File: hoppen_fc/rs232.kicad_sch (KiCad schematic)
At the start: 7 parts, among them U7 SP3223

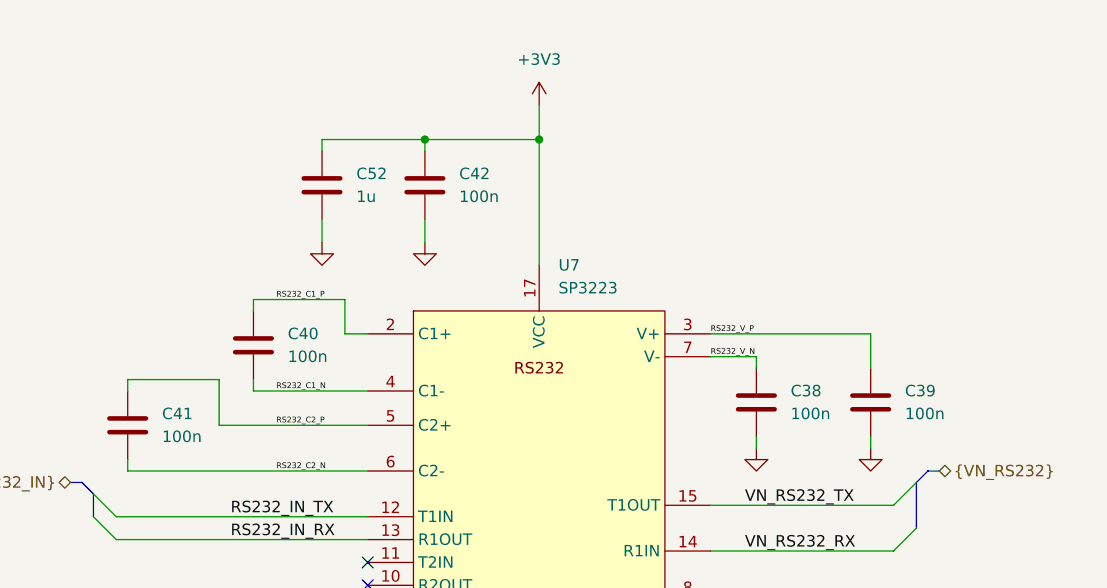
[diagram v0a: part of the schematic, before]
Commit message: finished adding lcsc numbers
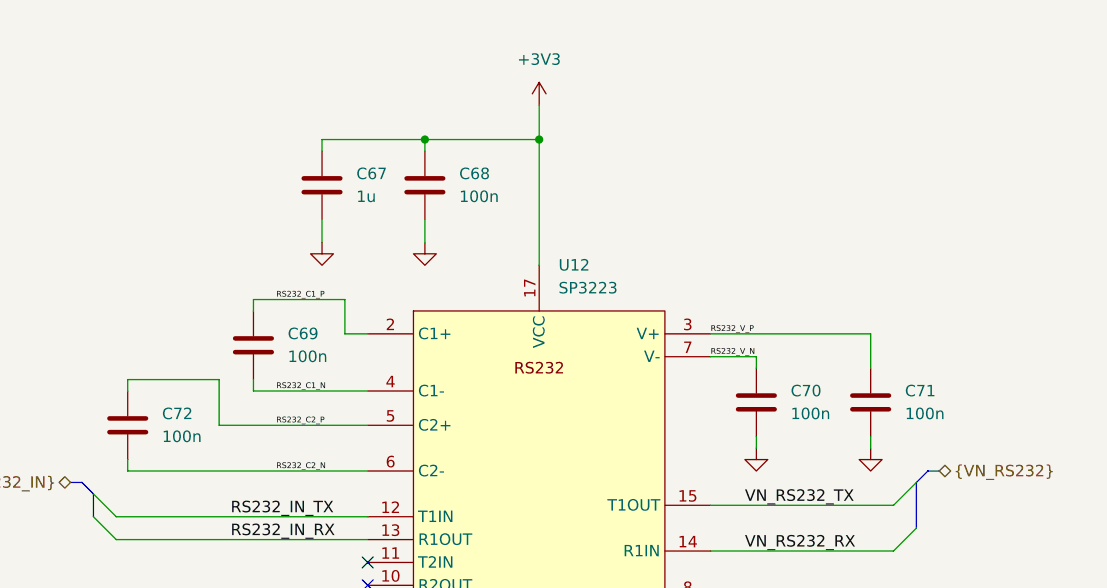
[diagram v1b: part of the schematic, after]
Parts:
- C67: renamed from C52; LCSC (none) -> C15849
- C68: renamed from C42; LCSC (none) -> C307331
- C69: renamed from C40; LCSC (none) -> C307331
- C70: renamed from C38; LCSC (none) -> C307331
- C71: renamed from C39; LCSC (none) -> C307331
- C72: renamed from C41; LCSC (none) -> C307331
- renumbered U7 to U12
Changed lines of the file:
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@@
 		(dnp no)
 		(fields_autoplaced yes)
-		(property "Reference" "C41"
+		(property "Reference" "C72"
 			(at 97.79 90.1699 0)
 			(effects
@@
 			)
 		)
+		(property "LCSC" "C307331"
+			(at 93.98 91.44 0)
+			(effects
+				(font
+					(size 1.27 1.27)
+				)
+				(hide yes)
+			)
+		)
 		(pin "2"
 		)
@@
 			(project "hoppen_fc"
 				(path "/abe950a1-9eef-4508-9fd4-31d3e723e029/c85454e5-a89e-41eb-a5ed-71b4fc4cf13a/b20bfd16-8587-4ee2-a4b4-53d6b6d5b5b2"
-					(reference "C41")
+					(reference "C72")
 					(unit 1)
 				)
@@
 		(dnp no)
 		(fields_autoplaced yes)
-		(property "Reference" "C40"
+		(property "Reference" "C69"
 			(at 111.76 81.2799 0)
 			(effects
@@
 			)
 		)
+		(property "LCSC" "C307331"
+			(at 107.95 82.55 0)
+			(effects
+				(font
+					(size 1.27 1.27)
+				)
+				(hide yes)
+			)
+		)
 		(pin "2"
 		)
@@
 			(project "hoppen_fc"
 				(path "/abe950a1-9eef-4508-9fd4-31d3e723e029/c85454e5-a89e-41eb-a5ed-71b4fc4cf13a/b20bfd16-8587-4ee2-a4b4-53d6b6d5b5b2"
-					(reference "C40")
+					(reference "C69")
 					(unit 1)
 				)
@@
 		(dnp no)
 		(fields_autoplaced yes)
-		(property "Reference" "#PWR051"
+		(property "Reference" "#PWR0105"
 			(at 176.53 100.33 0)
 			(effects
@@
 			(project "hoppen_fc"
 				(path "/abe950a1-9eef-4508-9fd4-31d3e723e029/c85454e5-a89e-41eb-a5ed-71b4fc4cf13a/b20bfd16-8587-4ee2-a4b4-53d6b6d5b5b2"
-					(reference "#PWR051")
+					(reference "#PWR0105")
 					(unit 1)
 				)
@@
 		(dnp no)
 		(fields_autoplaced yes)
-		(property "Reference" "C42"
+		(property "Reference" "C68"
 			(at 130.81 63.4999 0)
 			(effects
@@
 			)
 		)
+		(property "LCSC" "C307331"
+			(at 127 64.77 0)
+			(effects
+				(font
+					(size 1.27 1.27)
+				)
+				(hide yes)
+			)
+		)
 		(pin "2"
 		)
@@
 			(project "hoppen_fc"
 				(path "/abe950a1-9eef-4508-9fd4-31d3e723e029/c85454e5-a89e-41eb-a5ed-71b4fc4cf13a/b20bfd16-8587-4ee2-a4b4-53d6b6d5b5b2"
-					(reference "C42")
+					(reference "C68")
 					(unit 1)
 				)
@@
 		(dnp no)
 		(fields_autoplaced yes)
-		(property "Reference" "C38"
+		(property "Reference" "C70"
 			(at 167.64 87.6299 0)
 			(effects
@@
 			)
 		)
+		(property "LCSC" "C307331"
+			(at 163.83 88.9 0)
+			(effects
+				(font
+					(size 1.27 1.27)
+				)
+				(hide yes)
+			)
+		)
 		(pin "2"
 		)
@@
 			(project "hoppen_fc"
 				(path "/abe950a1-9eef-4508-9fd4-31d3e723e029/c85454e5-a89e-41eb-a5ed-71b4fc4cf13a/b20bfd16-8587-4ee2-a4b4-53d6b6d5b5b2"
-					(reference "C38")
+					(reference "C70")
 					(unit 1)
 				)
@@
 		(dnp no)
 		(fields_autoplaced yes)
-		(property "Reference" "#PWR050"
+		(property "Reference" "#PWR0104"
 			(at 163.83 100.33 0)
 			(effects
@@
 			(project ""
 				(path "/abe950a1-9eef-4508-9fd4-31d3e723e029/c85454e5-a89e-41eb-a5ed-71b4fc4cf13a/b20bfd16-8587-4ee2-a4b4-53d6b6d5b5b2"
-					(reference "#PWR050")
+					(reference "#PWR0104")
 					(unit 1)
 				)
@@
 		(dnp no)
 		(fields_autoplaced yes)
-		(property "Reference" "#PWR052"
+		(property "Reference" "#PWR0106"
 			(at 139.7 132.08 0)
 			(effects
@@
 			(project "hoppen_fc"
 				(path "/abe950a1-9eef-4508-9fd4-31d3e723e029/c85454e5-a89e-41eb-a5ed-71b4fc4cf13a/b20bfd16-8587-4ee2-a4b4-53d6b6d5b5b2"
-					(reference "#PWR052")
+					(reference "#PWR0106")
 					(unit 1)
 				)
@@
 		(dnp no)
 		(fields_autoplaced yes)
-		(property "Reference" "#PWR053"
+		(property "Reference" "#PWR0101"
 			(at 139.7 59.69 0)
 			(effects
@@
 			(project "hoppen_fc"
 				(path "/abe950a1-9eef-4508-9fd4-31d3e723e029/c85454e5-a89e-41eb-a5ed-71b4fc4cf13a/b20bfd16-8587-4ee2-a4b4-53d6b6d5b5b2"
-					(reference "#PWR053")
+					(reference "#PWR0101")
 					(unit 1)
 				)
@@
 		(dnp no)
 		(fields_autoplaced yes)
-		(property "Reference" "U7"
+		(property "Reference" "U12"
 			(at 141.8433 73.66 0)
 			(effects
@@
 			(project ""
 				(path "/abe950a1-9eef-4508-9fd4-31d3e723e029/c85454e5-a89e-41eb-a5ed-71b4fc4cf13a/b20bfd16-8587-4ee2-a4b4-53d6b6d5b5b2"
-					(reference "U7")
+					(reference "U12")
 					(unit 1)
 				)
@@
 		(dnp no)
 		(fields_autoplaced yes)
-		(property "Reference" "#PWR054"
+		(property "Reference" "#PWR0103"
 			(at 127 77.47 0)
 			(effects
@@
 			(project "hoppen_fc"
 				(path "/abe950a1-9eef-4508-9fd4-31d3e723e029/c85454e5-a89e-41eb-a5ed-71b4fc4cf13a/b20bfd16-8587-4ee2-a4b4-53d6b6d5b5b2"
-					(reference "#PWR054")
+					(reference "#PWR0103")
 					(unit 1)
 				)
@@
 		(dnp no)
 		(fields_autoplaced yes)
-		(property "Reference" "#PWR083"
+		(property "Reference" "#PWR0102"
 			(at 115.57 77.47 0)
 			(effects
@@
 			(project "hoppen_fc"
 				(path "/abe950a1-9eef-4508-9fd4-31d3e723e029/c85454e5-a89e-41eb-a5ed-71b4fc4cf13a/b20bfd16-8587-4ee2-a4b4-53d6b6d5b5b2"
-					(reference "#PWR083")
+					(reference "#PWR0102")
 					(unit 1)
 				)
@@
 		(dnp no)
 		(fields_autoplaced yes)
-		(property "Reference" "C39"
+		(property "Reference" "C71"
 			(at 180.34 87.6299 0)
 			(effects
@@
 			)
 		)
+		(property "LCSC" "C307331"
+			(at 176.53 88.9 0)
+			(effects
+				(font
+					(size 1.27 1.27)
+				)
+				(hide yes)
+			)
+		)
 		(pin "2"
 		)
@@
 			(project "hoppen_fc"
 				(path "/abe950a1-9eef-4508-9fd4-31d3e723e029/c85454e5-a89e-41eb-a5ed-71b4fc4cf13a/b20bfd16-8587-4ee2-a4b4-53d6b6d5b5b2"
-					(reference "C39")
+					(reference "C71")
 					(unit 1)
 				)
@@
 		(dnp no)
 		(fields_autoplaced yes)
-		(property "Reference" "C52"
+		(property "Reference" "C67"
 			(at 119.38 63.4999 0)
 			(effects
@@
 			)
 		)
+		(property "LCSC" "C15849"
+			(at 115.57 64.77 0)
+			(effects
+				(font
+					(size 1.27 1.27)
+				)
+				(hide yes)
+			)
+		)
 		(pin "1"
 		)
@@
 			(project "hoppen_fc"
 				(path "/abe950a1-9eef-4508-9fd4-31d3e723e029/c85454e5-a89e-41eb-a5ed-71b4fc4cf13a/b20bfd16-8587-4ee2-a4b4-53d6b6d5b5b2"
-					(reference "C52")
-					(unit 1)
-				)
+					(reference "C67")
+					(unit 1)
+				)

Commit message: ready for routing?
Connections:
- net RS232_nEN is gone; now on net RS232_C1_P: U12.1 (C1+)
- net +3V3: now also U12.16 (VCC); no longer U12.17 (VCC)
- net GND: now also U12.15 (GND); no longer U12.16 (GND)
- net RS232_C1_N: now also U12.3 (C1-); no longer U12.4 (C1-)
- net RS232_C1_P: no longer U12.2 (C1+)
- net RS232_C2_N: now also U12.5 (C2-); no longer U12.6 (C2-)
- net RS232_C2_P: now also U12.4 (C2+); no longer U12.5 (C2+)
- net RS232_IN_RX: now also U12.12 (R1OUT); no longer U12.13 (R1OUT)
- net RS232_IN_TX: now also U12.11 (T1IN); no longer U12.12 (T1IN)
- net RS232_V_N: now also U12.6 (V-); no longer U12.7 (V-)
- net RS232_V_P: now also U12.2 (V+); no longer U12.3 (V+)
- net VN_RS232_RX: now also U12.13 (R1IN); no longer U12.14 (R1IN)
- net VN_RS232_TX: now also U12.14 (T1OUT); no longer U12.15 (T1OUT)
- removed net RS232_nSHDN: U12.18 (nSHDN)
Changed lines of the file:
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@@
 	)
 	(no_connect
-		(at 120.65 106.68)
+		(at 120.65 110.49)
 	)
 	(no_connect
-		(at 120.65 109.22)
+		(at 120.65 115.57)
 	)
 	(no_connect
@@
 	)
 	(bus_entry
-		(at 90.17 99.06)
+		(at 90.17 97.79)
 		(size 2.54 2.54)
 		(stroke
@@
 	)
 	(bus_entry
-		(at 90.17 101.6)
+		(at 90.17 102.87)
 		(size 2.54 2.54)
 		(stroke
@@
 	(bus
 		(pts
-			(xy 87.63 97.79) (xy 88.9 97.79)
+			(xy 87.63 97.79) (xy 90.17 97.79)
 		)
 		(stroke
@@
 	(wire
 		(pts
-			(xy 92.71 101.6) (xy 120.65 101.6)
-		)
-		(stroke
-			(width 0)
-			(type default)
-		)
-	)
-	(wire
-		(pts
-			(xy 114.3 113.03) (xy 120.65 113.03)
+			(xy 92.71 100.33) (xy 120.65 100.33)
 		)
 		(stroke
@@
 	(wire
 		(pts
-			(xy 114.3 115.57) (xy 120.65 115.57)
-		)
-		(stroke
-			(width 0)
-			(type default)
-		)
-	)
-	(wire
-		(pts
 			(xy 176.53 81.28) (xy 176.53 85.09)
 		)
@@
 		)
 	)
+	(wire
+		(pts
+			(xy 107.95 77.47) (xy 118.11 77.47)
+		)
+		(stroke
+			(width 0)
+			(type default)
+		)
+	)
+	(wire
+		(pts
+			(xy 139.7 59.69) (xy 139.7 73.66)
+		)
+		(stroke
+			(width 0)
+			(type default)
+		)
+	)
+	(wire
+		(pts
+			(xy 107.95 78.74) (xy 107.95 77.47)
+		)
+		(stroke
+			(width 0)
+			(type default)
+		)
+	)
+	(wire
+		(pts
+			(xy 127 59.69) (xy 139.7 59.69)
+		)
+		(stroke
+			(width 0)
+			(type default)
+		)
+	)
+	(wire
+		(pts
+			(xy 127 68.58) (xy 127 71.12)
+		)
+		(stroke
+			(width 0)
+			(type default)
+		)
+	)
 	(bus
 		(pts
-			(xy 90.17 99.06) (xy 88.9 97.79)
-		)
-		(stroke
-			(width 0)
-			(type default)
-		)
-	)
-	(wire
-		(pts
-			(xy 107.95 77.47) (xy 118.11 77.47)
-		)
-		(stroke
-			(width 0)
-			(type default)
-		)
-	)
-	(wire
-		(pts
-			(xy 139.7 59.69) (xy 139.7 73.66)
-		)
-		(stroke
-			(width 0)
-			(type default)
-		)
-	)
-	(wire
-		(pts
-			(xy 107.95 78.74) (xy 107.95 77.47)
-		)
-		(stroke
-			(width 0)
-			(type default)
-		)
-	)
-	(wire
-		(pts
-			(xy 127 59.69) (xy 139.7 59.69)
-		)
-		(stroke
-			(width 0)
-			(type default)
-		)
-	)
-	(wire
-		(pts
-			(xy 127 68.58) (xy 127 71.12)
+			(xy 181.61 97.79) (xy 181.61 102.87)
+		)
+		(stroke
+			(width 0)
+			(type default)
+		)
+	)
+	(wire
+		(pts
+			(xy 115.57 59.69) (xy 127 59.69)
+		)
+		(stroke
+			(width 0)
+			(type default)
+		)
+	)
+	(wire
+		(pts
+			(xy 158.75 105.41) (xy 179.07 105.41)
+		)
+		(stroke
+			(width 0)
+			(type default)
+		)
+	)
+	(wire
+		(pts
+			(xy 93.98 86.36) (xy 93.98 87.63)
 		)
 		(stroke
@@
 	(bus
 		(pts
-			(xy 181.61 97.79) (xy 181.61 102.87)
-		)
-		(stroke
-			(width 0)
-			(type default)
-		)
-	)
-	(wire
-		(pts
-			(xy 115.57 59.69) (xy 127 59.69)
-		)
-		(stroke
-			(width 0)
-			(type default)
-		)
-	)
-	(wire
-		(pts
-			(xy 158.75 105.41) (xy 179.07 105.41)
-		)
-		(stroke
-			(width 0)
-			(type default)
-		)
-	)
-	(wire
-		(pts
-			(xy 93.98 86.36) (xy 93.98 87.63)
-		)
-		(stroke
-			(width 0)
-			(type default)
-		)
-	)
-	(bus
-		(pts
-			(xy 90.17 99.06) (xy 90.17 101.6)
+			(xy 90.17 97.79) (xy 90.17 102.87)
 		)
 		(stroke
@@
 	(wire
 		(pts
-			(xy 92.71 104.14) (xy 120.65 104.14)
+			(xy 92.71 105.41) (xy 120.65 105.41)
 		)
 		(stroke
@@
 	)
 	(label "RS232_IN_RX"
-		(at 105.41 104.14 0)
+		(at 105.41 105.41 0)
 		(effects
 			(font
@@
 	)
 	(label "RS232_IN_TX"
-		(at 105.41 101.6 0)
+		(at 105.41 100.33 0)
 		(effects
 			(font
@@
 			)
 			(justify left bottom)
-		)
-	)
-	(hierarchical_label "RS232_nSHDN"
-		(shape input)
-		(at 114.3 113.03 180)
-		(effects
-			(font
-				(size 1.27 1.27)
-			)
-			(justify right)
 		)
 	)
@@
 			)
 			(justify left)
-		)
-	)
-	(hierarchical_label "RS232_nEN"
-		(shape input)
-		(at 114.3 115.57 180)
-		(effects
-			(font
-				(size 1.27 1.27)
-			)
-			(justify right)
 		)
 	)
@@
 		(pin "6"
 		)
-		(pin "18"
-		)
 		(pin "1"
 		)
-		(pin "17"
-		)
 		(pin "10"

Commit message: comments
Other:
- note added: "ADD TVS DIODES"
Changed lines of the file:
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@@
+		)
+	)
+	(text "ADD TVS DIODES\n"
+		(exclude_from_sim no)
+		(at 89.916 46.228 0)
+		(effects
+			(font
+				(face "KiCad Font")
+				(size 2.54 2.54)
+				(thickness 0.508)
+				(bold yes)
+				(color 255 0 0 1)
+			)
 		)
 	)

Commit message: bump
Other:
- note removed: "ADD TVS DIODES"
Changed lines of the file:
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@@
-		)
-	)
-	(text "ADD TVS DIODES\n"
-		(exclude_from_sim no)
-		(at 89.916 46.228 0)
-		(effects
-			(font
-				(face "KiCad Font")
-				(size 2.54 2.54)
-				(thickness 0.508)
-				(bold yes)
-				(color 255 0 0 1)
-			)
 		)
 	)
